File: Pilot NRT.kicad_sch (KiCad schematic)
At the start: 71 parts, among them J1 Touchscreen, J10 Conn_01x02, J11 Conn_01x02, J12 Conn_01x02, J13 3.5'' LCD, J14 USB_B_Micro, J2 Conn_01x02, J3 Conn_01x02, J4 Conn_01x02, J5 Conn_01x02, J6 Conn_01x02, J7 Conn_01x02, J8 Conn_01x02, J9 Conn_01x02, SW1 SW_SPDT, SW2 SW_SPDT, U1 STM32F103CBT6, U2 W25X40CLSS, U3 AT24CS01-XHM, U4 USBLC6-2SC6, Y1 8MHz

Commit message: rouch parts placement
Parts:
- R24: footprint Resistor_SMD:R_0201_0603Metric -> flash_cs
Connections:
- net BACK_BUTTON: now also U1.25 (PB12); no longer U1.26 (PB13)
- net FLASH_CS: now also U1.22 (PB11)
- net HOME_BUTTON: now also U1.28 (PB15); no longer U1.25 (PB12)
- net PAGE_DOWN_BUTTON: now also U1.26 (PB13); no longer U1.27 (PB14)
- net PAGE_UP_BUTTON: now also U1.27 (PB14); no longer U1.28 (PB15)
- no-connect marks 9 -> 8
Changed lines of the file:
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@@
 	)
 	(no_connect
-		(at 71.12 163.83)
-	)
-	(no_connect
 		(at 266.7 135.89)
 	)
@@
 		)
 	)
-	(global_label "BACK_BUTTON"
-		(shape input)
-		(at 71.12 168.91 180)
-		(fields_autoplaced yes)
-		(effects
-			(font
-				(size 1.27 1.27)
-			)
-			(justify right)
-		)
-		(property "Intersheetrefs" "${INTERSHEET_REFS}"
-			(at 55.0719 168.91 0)
-			(effects
-				(font
-					(size 1.27 1.27)
-				)
-				(justify right)
-				(hide yes)
-			)
-		)
-	)
 	(global_label "LEFT_BUTTON"
 		(shape input)
@@
 		)
 	)
-	(global_label "PAGE_DOWN_BUTTON"
-		(shape input)
-		(at 71.12 171.45 180)
-		(fields_autoplaced yes)
-		(effects
-			(font
-				(size 1.27 1.27)
-			)
-			(justify right)
-		)
-		(property "Intersheetrefs" "${INTERSHEET_REFS}"
-			(at 48.8429 171.45 0)
-			(effects
-				(font
-					(size 1.27 1.27)
-				)
-				(justify right)
-				(hide yes)
-			)
-		)
-	)
 	(global_label "DOWN_BUTTON"
 		(shape input)
@@
 		)
 	)
-	(global_label "HOME_BUTTON"
+	(global_label "RIGHT_BUTTON"
 		(shape input)
-		(at 71.12 166.37 180)
+		(at 153.67 73.66 180)
 		(fields_autoplaced yes)
 		(effects
@@
 		)
 		(property "Intersheetrefs" "${INTERSHEET_REFS}"
-			(at 54.7091 166.37 0)
+			(at 137.0776 73.66 0)
 			(effects
 				(font
@@
 		)
 	)
-	(global_label "RIGHT_BUTTON"
+	(global_label "LCD_RESET"
 		(shape input)
-		(at 153.67 73.66 180)
+		(at 269.24 29.21 180)
 		(fields_autoplaced yes)
 		(effects
@@
 		)
 		(property "Intersheetrefs" "${INTERSHEET_REFS}"
-			(at 137.0776 73.66 0)
+			(at 255.974 29.21 0)
 			(effects
 				(font
@@
 		)
 	)
-	(global_label "LCD_RESET"
+	(global_label "OK_BUTTON"
 		(shape input)
-		(at 269.24 29.21 180)
+		(at 204.47 96.52 180)
 		(fields_autoplaced yes)
 		(effects
@@
 		)
 		(property "Intersheetrefs" "${INTERSHEET_REFS}"
-			(at 255.974 29.21 0)
+			(at 190.72 96.52 0)
 			(effects
 				(font
@@
 		)
 	)
-	(global_label "OK_BUTTON"
+	(global_label "USB1_CONN+"
 		(shape input)
-		(at 204.47 96.52 180)
+		(at 200.66 135.89 180)
 		(fields_autoplaced yes)
 		(effects
@@
 		)
 		(property "Intersheetrefs" "${INTERSHEET_REFS}"
-			(at 190.72 96.52 0)
+			(at 184.8538 135.89 0)
 			(effects
 				(font
@@
 		)
 	)
-	(global_label "USB1_CONN+"
+	(global_label "FLASH_CS"
 		(shape input)
-		(at 200.66 135.89 180)
+		(at 71.12 163.83 180)
 		(fields_autoplaced yes)
 		(effects
@@
 		)
 		(property "Intersheetrefs" "${INTERSHEET_REFS}"
-			(at 184.8538 135.89 0)
+			(at 58.9424 163.83 0)
 			(effects
 				(font
@@
 		)
 	)
+	(global_label "PAGE_UP_BUTTON"
+		(shape input)
+		(at 71.12 171.45 180)
+		(fields_autoplaced yes)
+		(effects
+			(font
+				(size 1.27 1.27)
+			)
+			(justify right)
+		)
+		(property "Intersheetrefs" "${INTERSHEET_REFS}"
+			(at 51.6248 171.45 0)
+			(effects
+				(font
+					(size 1.27 1.27)
+				)
+				(justify right)
+				(hide yes)
+			)
+		)
+	)
 	(global_label "TOUCHSCREEN_RESET"
 		(shape input)
@@
 		)
 	)
-	(global_label "PAGE_UP_BUTTON"
-		(shape input)
-		(at 71.12 173.99 180)
-		(fields_autoplaced yes)
-		(effects
-			(font
-				(size 1.27 1.27)
-			)
-			(justify right)
-		)
-		(property "Intersheetrefs" "${INTERSHEET_REFS}"
-			(at 51.6248 173.99 0)
-			(effects
-				(font
-					(size 1.27 1.27)
-				)
-				(justify right)
-				(hide yes)
-			)
-		)
-	)
 	(global_label "ON_BUTTON"
 		(shape input)
@@
 		)
 	)
+	(global_label "BACK_BUTTON"
+		(shape input)
+		(at 71.12 166.37 180)
+		(fields_autoplaced yes)
+		(effects
+			(font
+				(size 1.27 1.27)
+			)
+			(justify right)
+		)
+		(property "Intersheetrefs" "${INTERSHEET_REFS}"
+			(at 55.0719 166.37 0)
+			(effects
+				(font
+					(size 1.27 1.27)
+				)
+				(justify right)
+				(hide yes)
+			)
+		)
+	)
 	(global_label "I2C1_SCL"
 		(shape input)
@@
 		)
 	)
+	(global_label "HOME_BUTTON"
+		(shape input)
+		(at 71.12 173.99 180)
+		(fields_autoplaced yes)
+		(effects
+			(font
+				(size 1.27 1.27)
+			)
+			(justify right)
+		)
+		(property "Intersheetrefs" "${INTERSHEET_REFS}"
+			(at 54.7091 173.99 0)
+			(effects
+				(font
+					(size 1.27 1.27)
+				)
+				(justify right)
+				(hide yes)
+			)
+		)
+	)
 	(global_label "I2C1_SDA"
 		(shape input)
@@
 		)
 	)
+	(global_label "PAGE_DOWN_BUTTON"
+		(shape input)
+		(at 71.12 168.91 180)
+		(fields_autoplaced yes)
+		(effects
+			(font
+				(size 1.27 1.27)
+			)
+			(justify right)
+		)
+		(property "Intersheetrefs" "${INTERSHEET_REFS}"
+			(at 48.8429 168.91 0)
+			(effects
+				(font
+					(size 1.27 1.27)
+				)
+				(justify right)
+				(hide yes)
+			)
+		)
+	)
 	(global_label "I2C1_SDA"
 		(shape input)
@@
 			)
 		)
-		(property "Footprint" "Resistor_SMD:R_0201_0603Metric"
+		(property "Footprint" "flash_cs"
 			(at 248.92 58.42 0)
 			(effects

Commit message: first wiring
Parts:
- C10, C9: footprint Capacitor_SMD:C_0201_0603Metric -> Capacitor_SMD:C_0402_1005Metric
- D1: footprint Capacitor_SMD:C_0201_0603Metric -> Diode_SMD:D_0603_1608Metric
- R22, R23, R25: footprint Resistor_SMD:R_0201_0603Metric -> Resistor_SMD:R_0603_1608Metric
- R24: footprint flash_cs -> Resistor_SMD:R_0603_1608Metric
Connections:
- net +3.3VA: no longer C7.1, C8.1, L1.2
- net BACK_BUTTON: now also U1.14 (PA4); no longer U1.25 (PB12)
- net DOWN_BUTTON: now also U1.25 (PB12); no longer U1.12 (PA2)
- net HOME_BUTTON: now also U1.11 (PA1); no longer U1.28 (PB15)
- net LEFT_BUTTON: now also U1.28 (PB15); no longer U1.13 (PA3)
- net MENU_BUTTON: now also U1.10 (PA0); no longer U1.29 (PA8)
- net OK_BUTTON: now also U1.27 (PB14); no longer U1.14 (PA4)
- net PAGE_DOWN_BUTTON: now also U1.13 (PA3); no longer U1.26 (PB13)
- net PAGE_UP_BUTTON: now also U1.12 (PA2); no longer U1.27 (PB14)
- net RIGHT_BUTTON: now also U1.26 (PB13); no longer U1.11 (PA1)
- net UP_BUTTON: now also U1.29 (PA8); no longer U1.10 (PA0)
- new net +3.3VA_1: C7.1, C8.1, L1.2

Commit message: gerber files
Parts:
- C1, C11, C12, C13, C14, C15, C16, C17, C18, C19, C20, C21, C22, C23, C3, C4, C5, C6: LCSC Part # (none) -> C1525
- C10, C9: LCSC Part # (none) -> C1658
- C2: LCSC Part # (none) -> C19666
- C7: LCSC Part # (none) -> C77006
- C8: LCSC Part # (none) -> C15195
- D1: LCSC Part # (none) -> C2286
- J1: LCSC Part # (none) -> C161692
- J10, J11, J12, J2, J3, J4, J5, J6, J7, J8, J9: LCSC Part # (none) -> C161690
- J13: LCSC Part # (none) -> C265368
- J14: LCSC Part # (none) -> C114094
- L1: LCSC Part # (none) -> C408157
- R1, R2: LCSC Part # (none) -> C25879
- R10, R11, R12, R13, R14, R15, R16, R17, R18, R19, R20, R21, R4, R8: LCSC Part # (none) -> C25744
- R22: LCSC Part # (none) -> C21190
- R23, R24, R25: LCSC Part # (none) -> C22984
- R3, R5, R6: LCSC Part # (none) -> C25092
- R7: LCSC Part # (none) -> C25867
- R9: LCSC Part # (none) -> C17168
- SW1, SW2: LCSC Part # (none) -> C778186
- U1: LCSC Part # (none) -> C8304
- U2: LCSC Part # (none) -> C97521
- U3: LCSC Part # (none) -> C918274
- U4: LCSC Part # (none) -> C2827654
- Y1: LCSC Part # (none) -> C115962
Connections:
- net +3.3VA_1 is gone; now on net 3.3VA_1: C7.1, C8.1, L1.2
- net +3.3VA renamed 3.3VA_1

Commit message: fix wrong footprints
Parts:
- C10, C9: footprint Capacitor_SMD:C_0402_1005Metric -> Capacitor_SMD:C_0603_1608Metric
- J14: footprint Connector_USB:USB_Micro-B_Molex-105017-0001 -> kwrzesni:USB-B micro
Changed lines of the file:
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@@
 			)
 		)
-		(property "Footprint" "Connector_USB:USB_Micro-B_Molex-105017-0001"
+		(property "Footprint" "kwrzesni:USB-B micro"
 			(at 270.51 132.08 0)
 			(effects
@@
 			)
 		)
-		(property "Footprint" "Capacitor_SMD:C_0402_1005Metric"
+		(property "Footprint" "Capacitor_SMD:C_0603_1608Metric"
 			(at 162.56 26.67 0)
 			(effects
@@
 			)
 		)
-		(property "Footprint" "Capacitor_SMD:C_0402_1005Metric"
+		(property "Footprint" "Capacitor_SMD:C_0603_1608Metric"
 			(at 162.56 19.05 0)
 			(effects

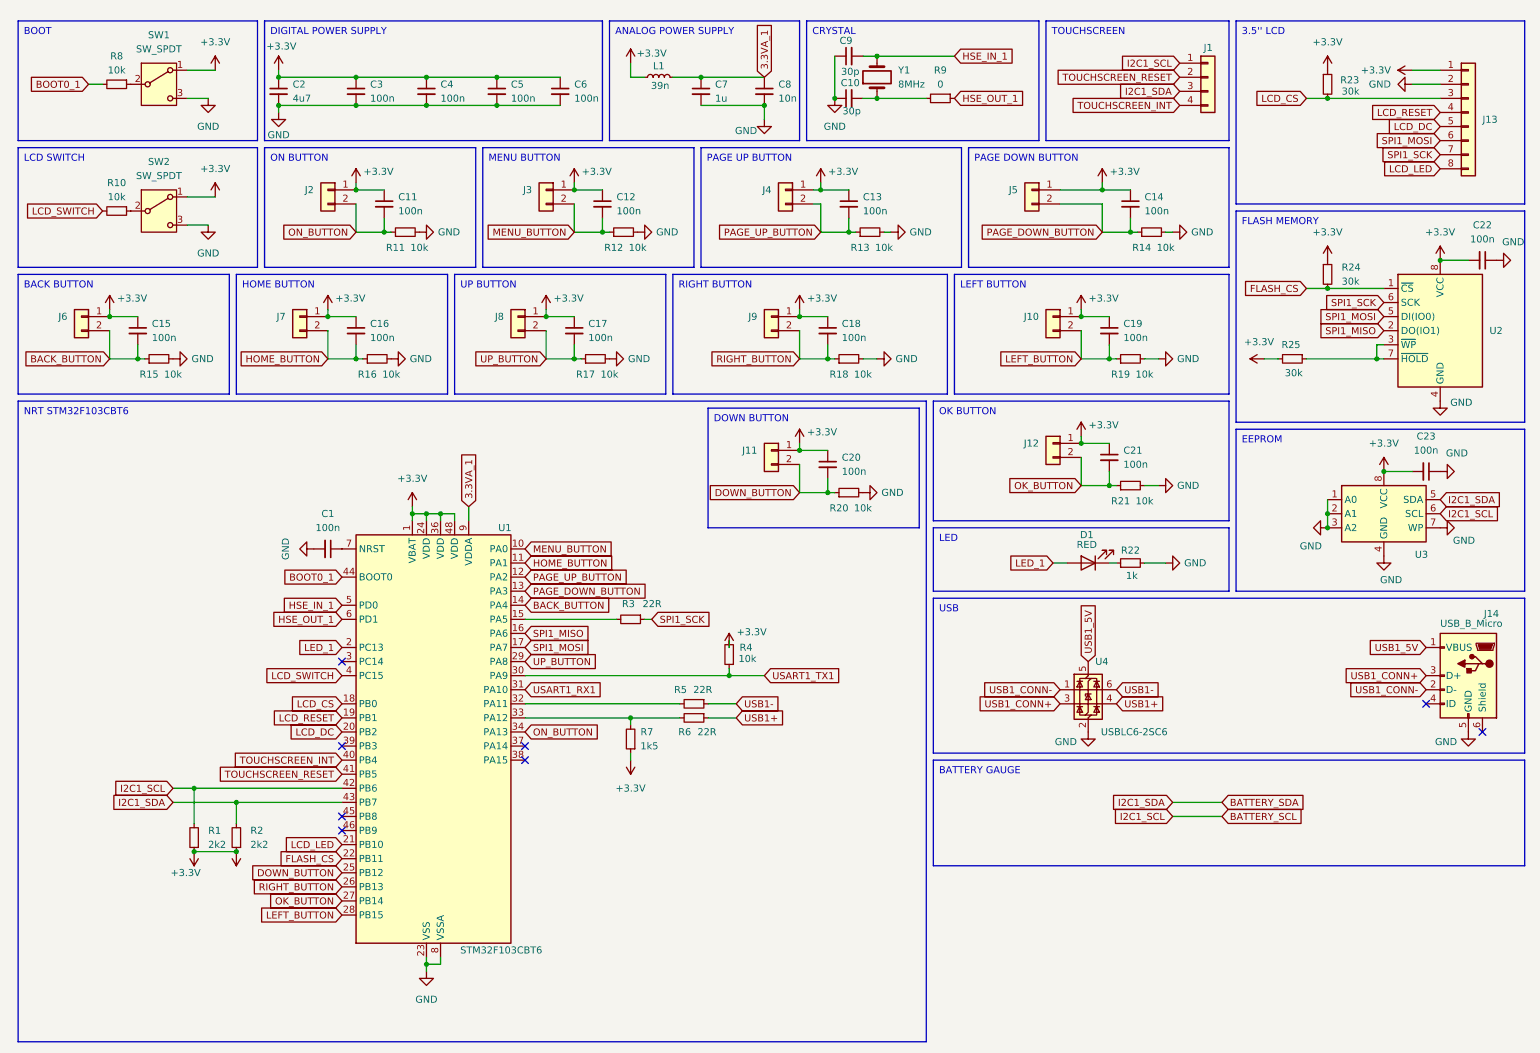
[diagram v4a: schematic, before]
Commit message: update to STM32F04
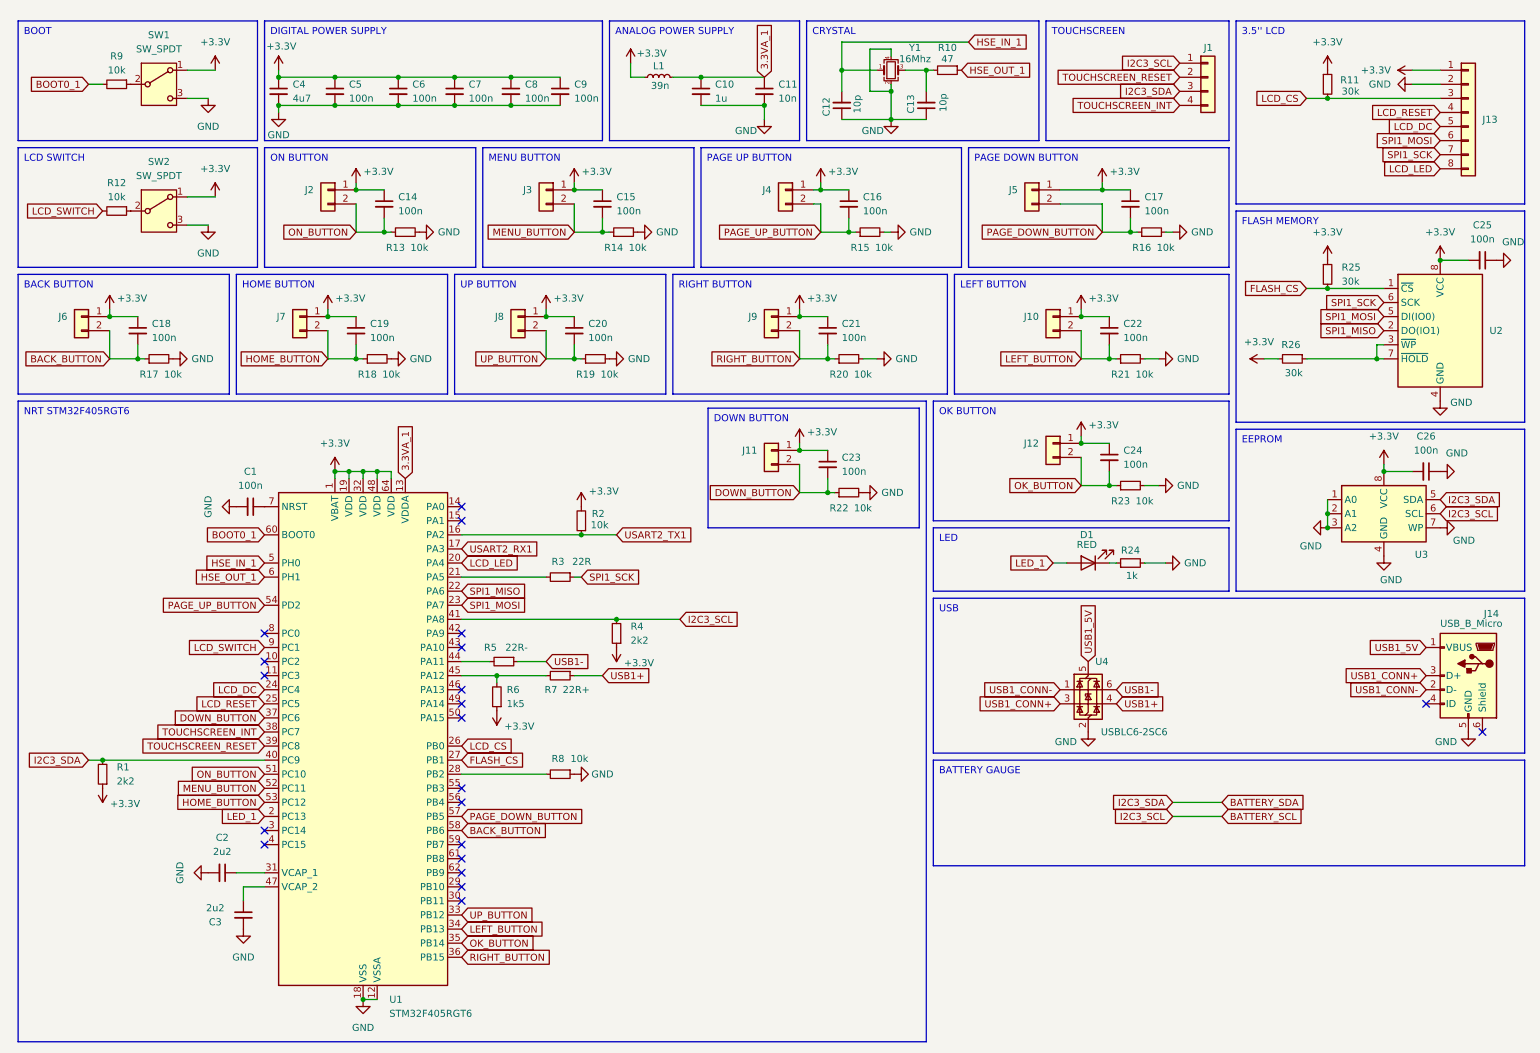
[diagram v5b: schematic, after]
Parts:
- removed U1: STM32F103CBT6, Package_QFP:LQFP-48_7x7mm_P0.5mm, symbol MCU_ST_STM32F1:STM32F103CBTx
- removed Y1: 8MHz, Crystal:Crystal_SMD_5032-2Pin_5.0x3.2mm, symbol Device:Crystal
- added C2, C3: 2u2, Capacitor_SMD:C_0603_1608Metric, symbol Device:C_Small
- added C9: 100n, Capacitor_SMD:C_0402_1005Metric, symbol Device:C_Small
- added R8: 10k, Resistor_SMD:R_0402_1005Metric, symbol Device:R_Small
- added U1: STM32F405RGT6, Package_QFP:LQFP-64_10x10mm_P0.5mm, symbol MCU_ST_STM32F4:STM32F405RGTx
- added Y1: 16Mhz, Crystal:Crystal_SMD_3225-4Pin_3.2x2.5mm, symbol Device:Crystal_GND24_Small
- C12: renamed from C9; value 30p -> 10p; footprint Capacitor_SMD:C_0603_1608Metric -> Capacitor_SMD:C_0402_1005Metric; LCSC Part # C1658 -> C650948
- C13: renamed from C10; value 30p -> 10p; footprint Capacitor_SMD:C_0603_1608Metric -> Capacitor_SMD:C_0402_1005Metric; LCSC Part # C1658 -> C650948
- R10: renamed from R9; value 0 -> 47; LCSC Part # C17168 -> C137864
- R2: value 2k2 -> 10k; LCSC Part # C25879 -> C25744
- R4: value 10k -> 2k2; LCSC Part # C25744 -> C25879
- R5: value 22R -> 22R-
- R6: value 22R -> 1k5; LCSC Part # C25092 -> C25867
- R7: value 1k5 -> 22R+; LCSC Part # C25867 -> C25092
- renumbered C7 to C10, C8 to C11, C11 to C14, C12 to C15, C13 to C16, C14 to C17, C15 to C18, C16 to C19, C17 to C20, C18 to C21, C19 to C22, C20 to C23, C21 to C24, C22 to C25, C23 to C26, C2 to C4, C3 to C5, C4 to C6, C5 to C7, C6 to C8, R23 to R11, R10 to R12, R11 to R13, R12 to R14, R13 to R15, R14 to R16, R15 to R17, R16 to R18, R17 to R19, R18 to R20, R19 to R21, R20 to R22, R21 to R23, R22 to R24, R24 to R25, R25 to R26, R8 to R9
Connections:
- net USART1_TX1 is gone; now on net +3.3V: R4.1
- net +3.3V: now also R2.2, R6.1, C9.1, U1.1 (VBAT), U1.19 (VDD), U1.32 (VDD), U1.48 (VDD), U1.64 (VDD); no longer R2.1, R4.2, R7.1
- net 3.3VA_1: now also U1.13 (VDDA)
- net BACK_BUTTON: now also U1.58 (PB6)
- net BATTERY_SCL: now also R4.2, U1.41 (PA8); no longer R1.2
- net BATTERY_SDA: now also R1.2, U1.40 (PC9); no longer R2.2
- net BOOT0_1: now also U1.60 (BOOT0)
- net DOWN_BUTTON: now also U1.37 (PC6)
- net FLASH_CS: now also U1.27 (PB1)
- net GND: now also C2.2, C3.2, C9.2, R8.1, U1.12 (VSSA), U1.18 (VSS), U1.63 (VSS), Y1.2, Y1.4
- net HOME_BUTTON: now also U1.53 (PC12)
- net HSE_IN_1: now also U1.5 (PH0), Y1.1
- net HSE_OUT_1: now also U1.6 (PH1)
- net LCD_CS: now also U1.26 (PB0)
- net LCD_DC: now also U1.24 (PC4)
- net LCD_LED: now also U1.20 (PA4)
- net LCD_RESET: now also U1.25 (PC5)
- net LCD_SWITCH: now also U1.9 (PC1)
- net LED_1: now also U1.2 (PC13)
- net LEFT_BUTTON: now also U1.34 (PB13)
- net MENU_BUTTON: now also U1.52 (PC11)
- net OK_BUTTON: now also U1.35 (PB14)
- net ON_BUTTON: now also U1.51 (PC10)
- net PAGE_DOWN_BUTTON: now also U1.57 (PB5)
- net PAGE_UP_BUTTON: now also U1.54 (PD2)
- net RIGHT_BUTTON: now also U1.36 (PB15)
- net SPI1_MISO: now also U1.22 (PA6)
- net SPI1_MOSI: now also U1.23 (PA7)
- net TOUCHSCREEN_INT: now also U1.38 (PC7)
- net TOUCHSCREEN_RESET: now also U1.39 (PC8)
- net UP_BUTTON: now also U1.33 (PB12)
- net USB1+: now also R7.1; no longer R6.1
- net at R3.2: now also U1.21 (PA5)
- net at C13.2, R10.2: now also Y1.3
- net at R6.2, R7.2: now also U1.45 (PA12)
- net at R5.2: now also U1.44 (PA11)
- net at C1.1: now also U1.7 (NRST)
- new net: C2.1, U1.31 (VCAP_1)
- new net: C3.1, U1.47 (VCAP_2)
- new net: R8.2, U1.28 (PB2)
- new net USART2_RX1: U1.17 (PA3)
- new net USART2_TX1: R2.1, U1.16 (PA2)
- no-connect marks 8 -> 21
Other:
- moved on the sheet: C12, C13, C5, C6, C7, C8, R10
